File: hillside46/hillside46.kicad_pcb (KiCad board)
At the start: 2 copper layers, 142.5 x 99.9 mm, 93 parts, among them J1 I2C, J2 TRRS, J3 Bat_Pos, J4 Bat_Neg, J5 XF2M-1215-1A, K1 SW_Key, K10 SW_Key, K11 SW_Key, K12 SW_Key, K13 SW_Key, K14 SW_Key, K15 SW_Key, K16 SW_Key, K17 SW_Key, K18 SW_Key, K19 SW_Rotary, K2 SW_Key, K20 SW_Rotary, K21 SW_Key, K22 SW_Key, K23 SW_Key, K3 SW_Key, K4 SW_Key, K5 SW_Key, K6 SW_Key, K7 SW_Key, K8 SW_Key, K9 SW_Key, SW1 SKQGAFE010, SW2 SW_Power, U1 NiceNano2_r, U2 SRV05-4

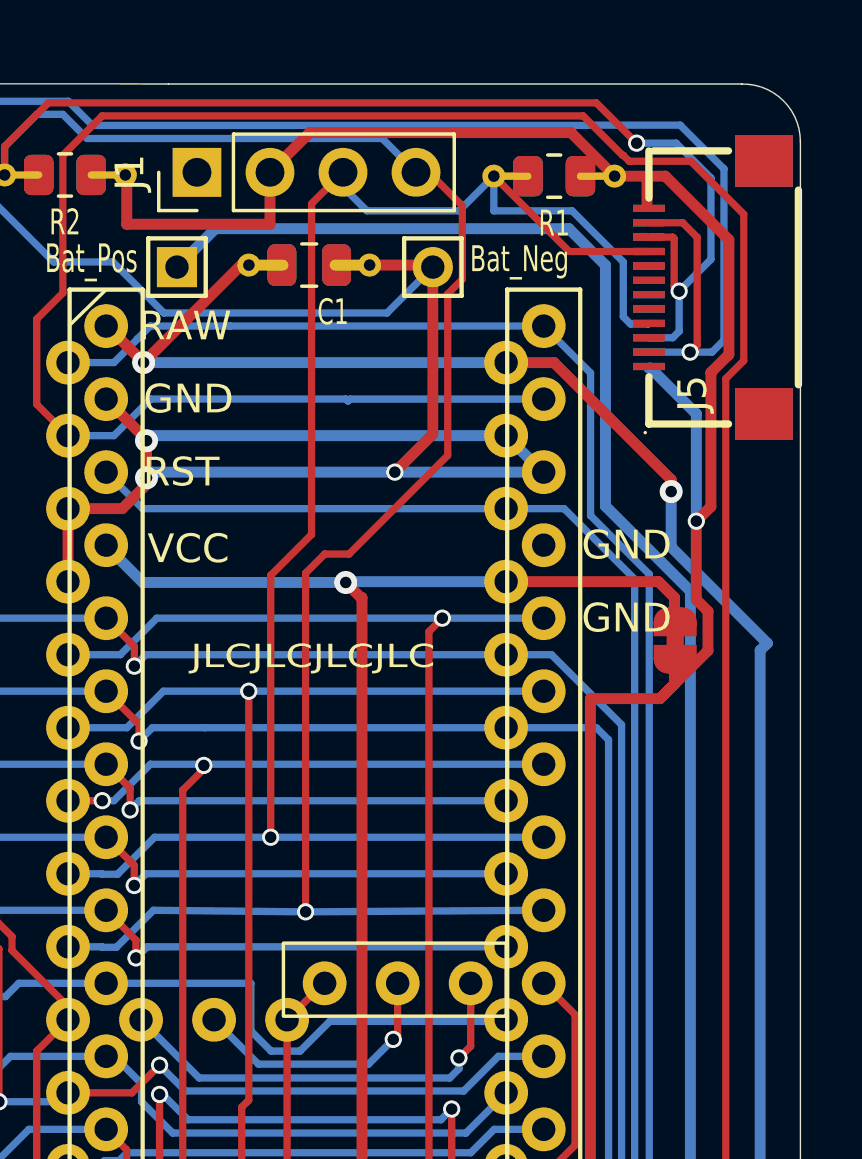
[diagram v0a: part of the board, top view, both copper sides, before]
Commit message: Connecting the data ready pin
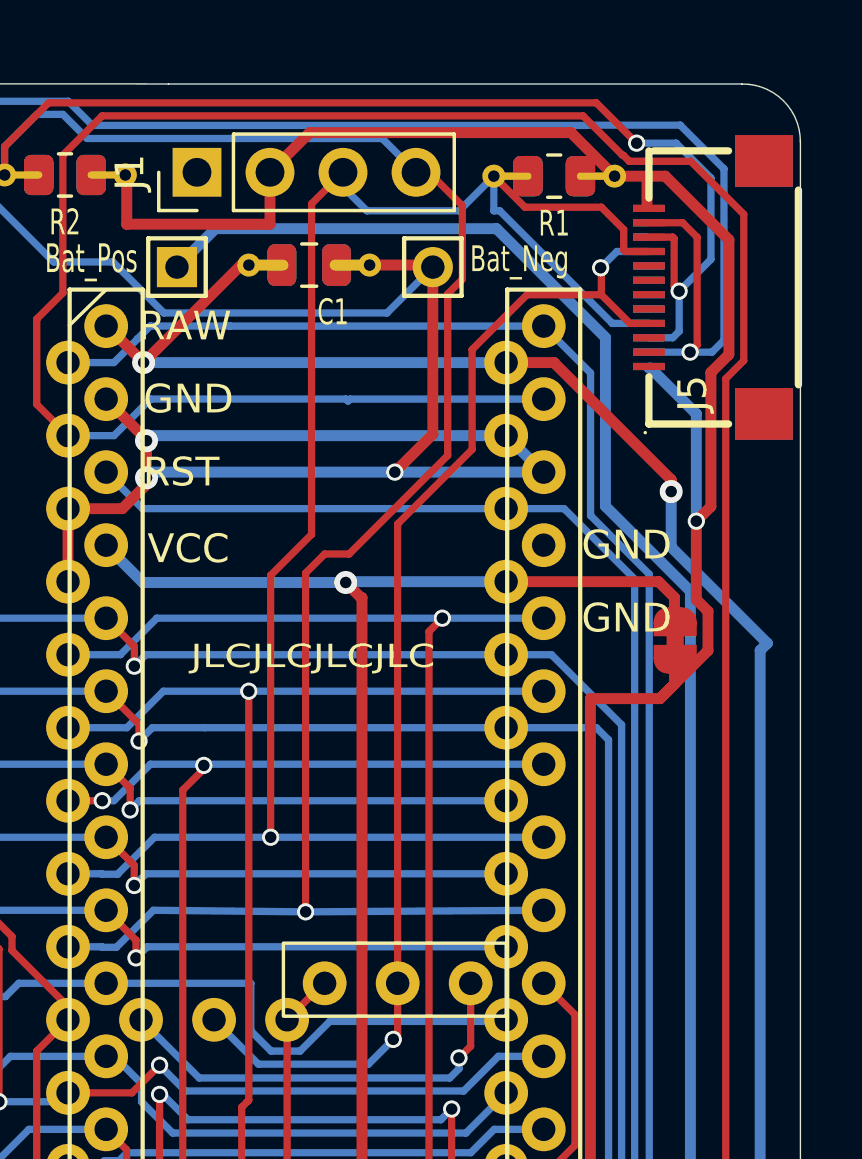
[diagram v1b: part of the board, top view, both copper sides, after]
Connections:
- J5 pad 4: unconnected-(J5-Pad4) -> DR
- U1 pad 26: unconnected-(U1-Pad26) -> DR
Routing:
- net DR: track 0.00 -> 42.6 mm, vias 0 -> 2
- net unconnected-(U1-Pad26): track 9.24 -> 0.00 mm, vias 1 -> 0
- net bat+: track 62.5 -> 61.0 mm
- net SCL: track 63.2 -> 62.5 mm

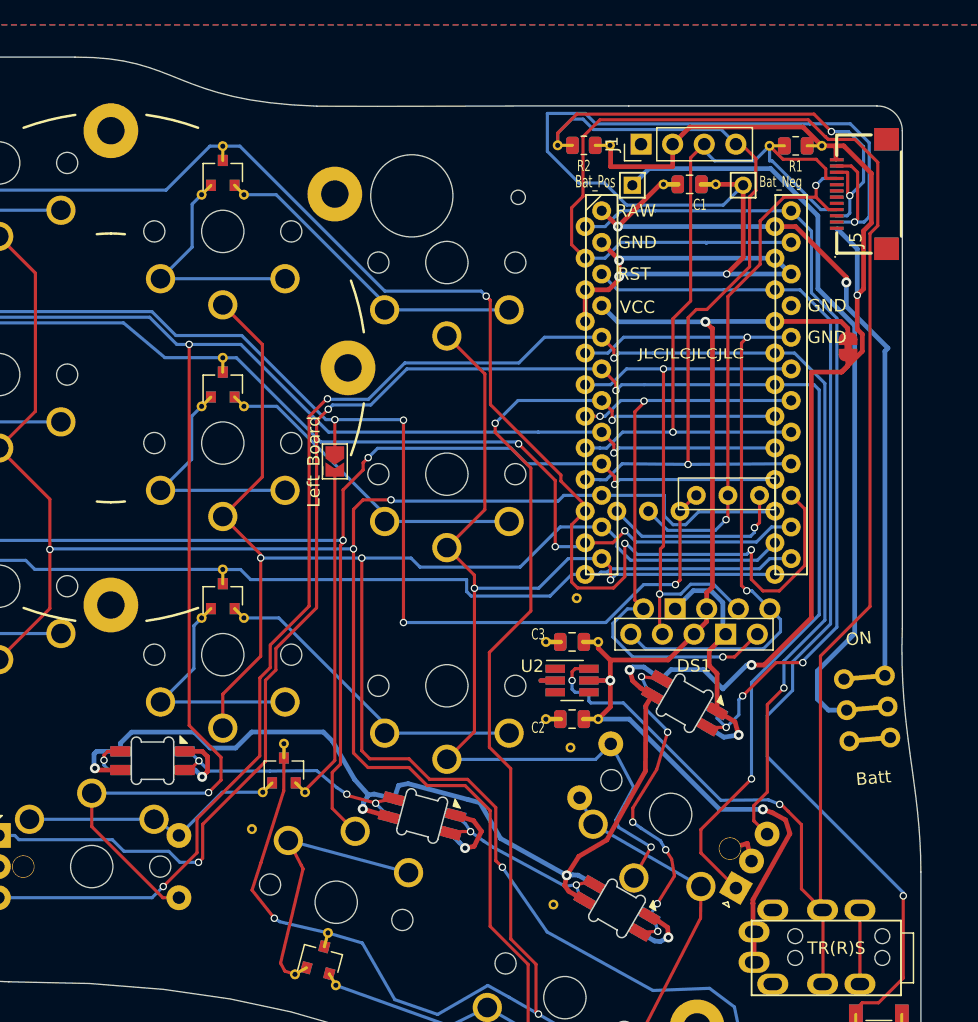
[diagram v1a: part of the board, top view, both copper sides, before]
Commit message: Flipping nice nano vias for bottom mount, removed I2C headers, moved edge cut closer to the nice nano edge
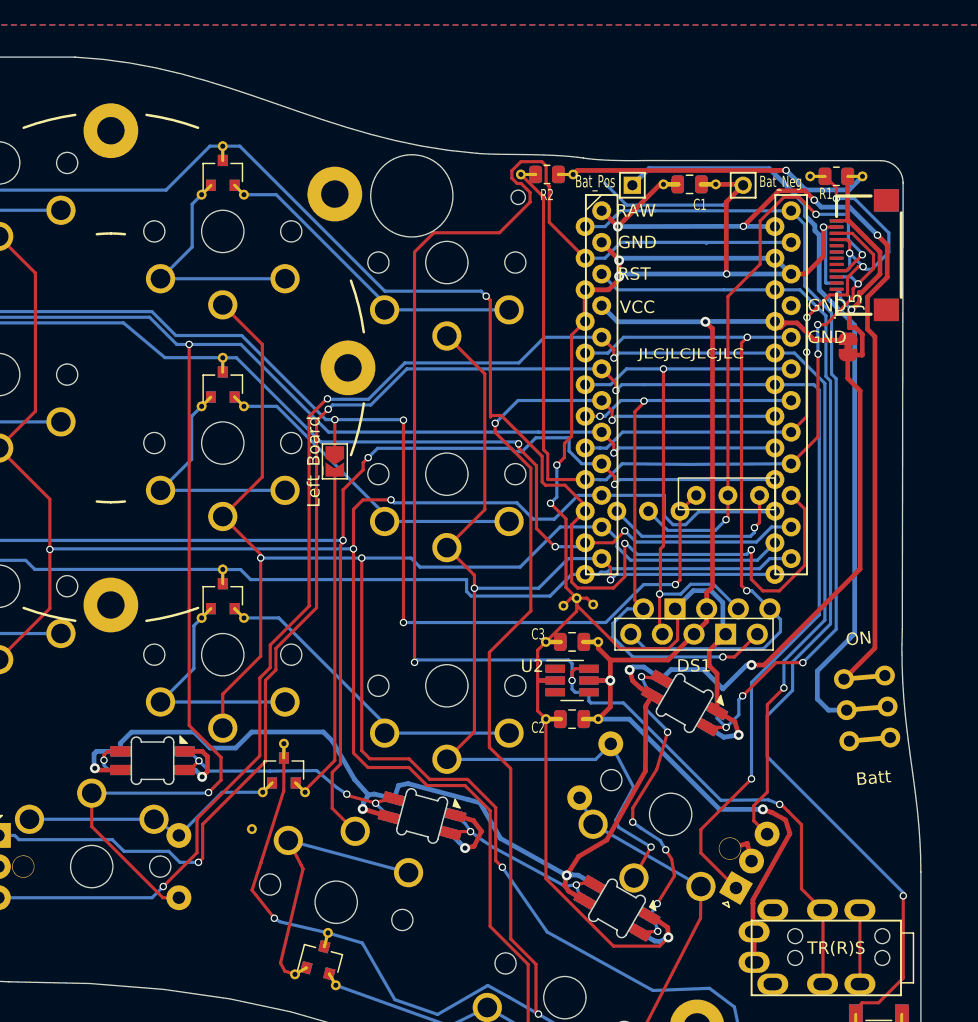
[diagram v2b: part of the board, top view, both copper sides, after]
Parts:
- removed J1: I2C, Connector_PinHeader_2.54mm:PinHeader_1x04_P2.54mm_Vertical
- moved V3 24.0 mm to (187.9, 84.8), turned to 0 degrees
- moved V1 11.6 mm to (190.2, 84.7)
- moved J5 4.90 mm to (212.4, 56.6)
- moved R1 4.08 mm to (209.8, 50.3)
- moved R2 3.77 mm to (186.5, 50.1)
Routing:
- net GND: track 151.9 -> 190.6 mm, vias 8 -> 10
- net SDA: track 99.6 -> 71.1 mm
- net data: track 154.5 -> 129.9 mm, vias 2 -> 3
- net SCL: track 62.5 -> 51.5 mm, vias 1 -> 5
- net raw: track 60.4 -> 70.8 mm, vias 2 -> 4
- net VCC_ACC: track 170.5 -> 165.1 mm, vias 6 -> 7
- net DR: track 42.6 -> 48.0 mm, vias 2 -> 3
- net row0: track 153.0 -> 154.6 mm
- net col2: track 150.1 -> 151.7 mm
- net col3: track 154.8 -> 156.0 mm
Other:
- outline, holes or cut-outs redrawn

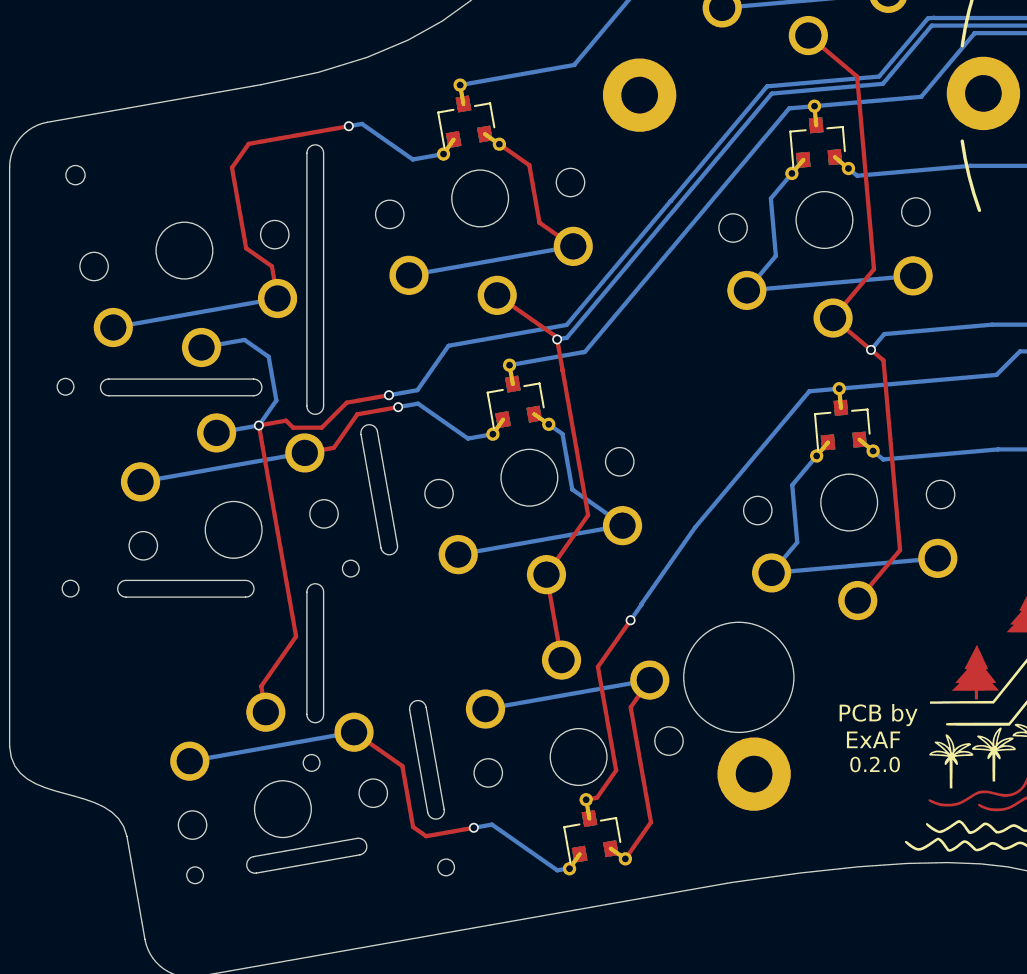
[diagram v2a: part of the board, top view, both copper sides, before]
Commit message: Updating pinky column cutouts to be aligned with pinky switches
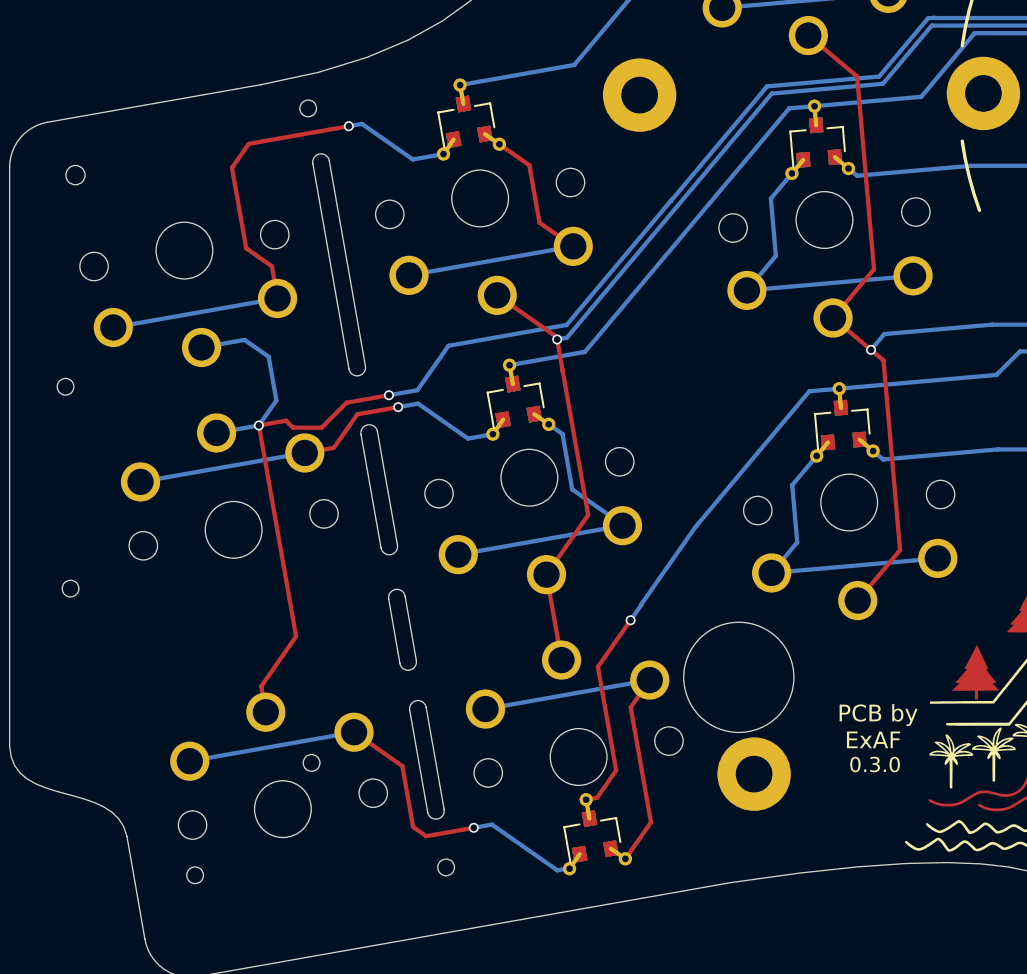
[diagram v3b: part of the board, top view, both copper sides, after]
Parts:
- moved H31 27.7 mm to (92.0, 66.5)
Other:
- outline, holes or cut-outs redrawn
- board text added: "-cut 4-"
- board text added: "-cut 5-"
- board text added: "0.3.0"
- board text removed: "-2-"
- board text removed: "-br-"
- board text removed: "-cut A-"
- board text removed: "-cut Z-"
- board text removed: "0.2.0"
- board text removed: "cut Y-"
